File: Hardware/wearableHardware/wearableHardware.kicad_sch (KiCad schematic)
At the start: 0 parts

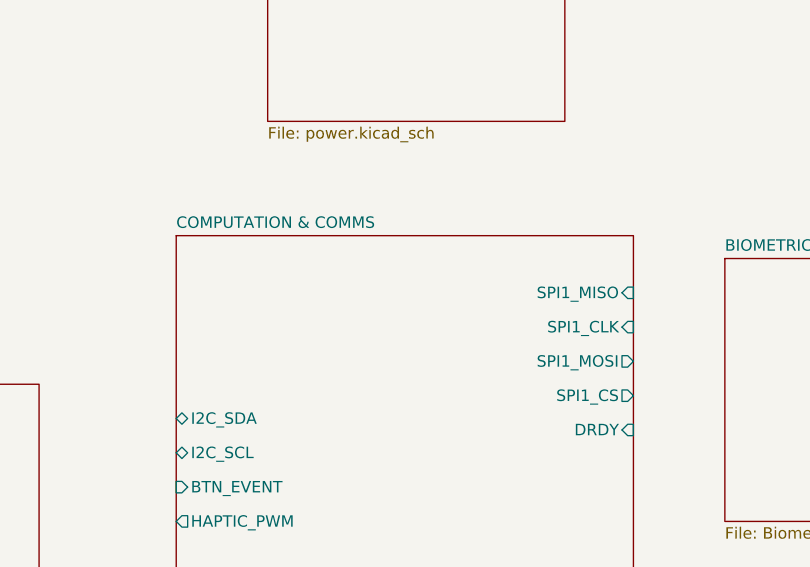
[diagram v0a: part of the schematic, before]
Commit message: feat: initialize KiCad hardware project with MCU schematic and pinmap configuration
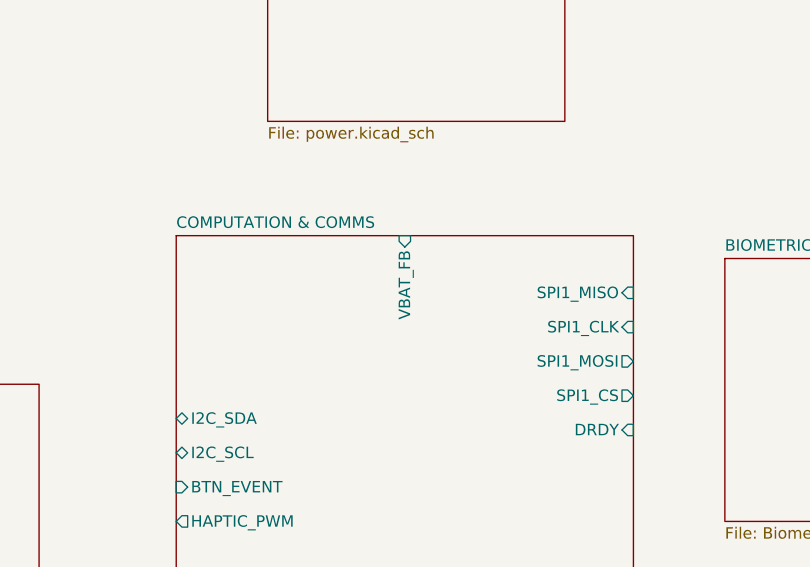
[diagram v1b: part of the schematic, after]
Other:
- sheet COMPUTATION & COMMS ports: added VBAT_FB; removed none
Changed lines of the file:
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@@
+			)
+		)
+		(pin "VBAT_FB" input
+			(at 128.27 58.42 90)
+			(effects
+				(font
+					(size 1.27 1.27)
+				)
+				(justify right)
 			)
 		)

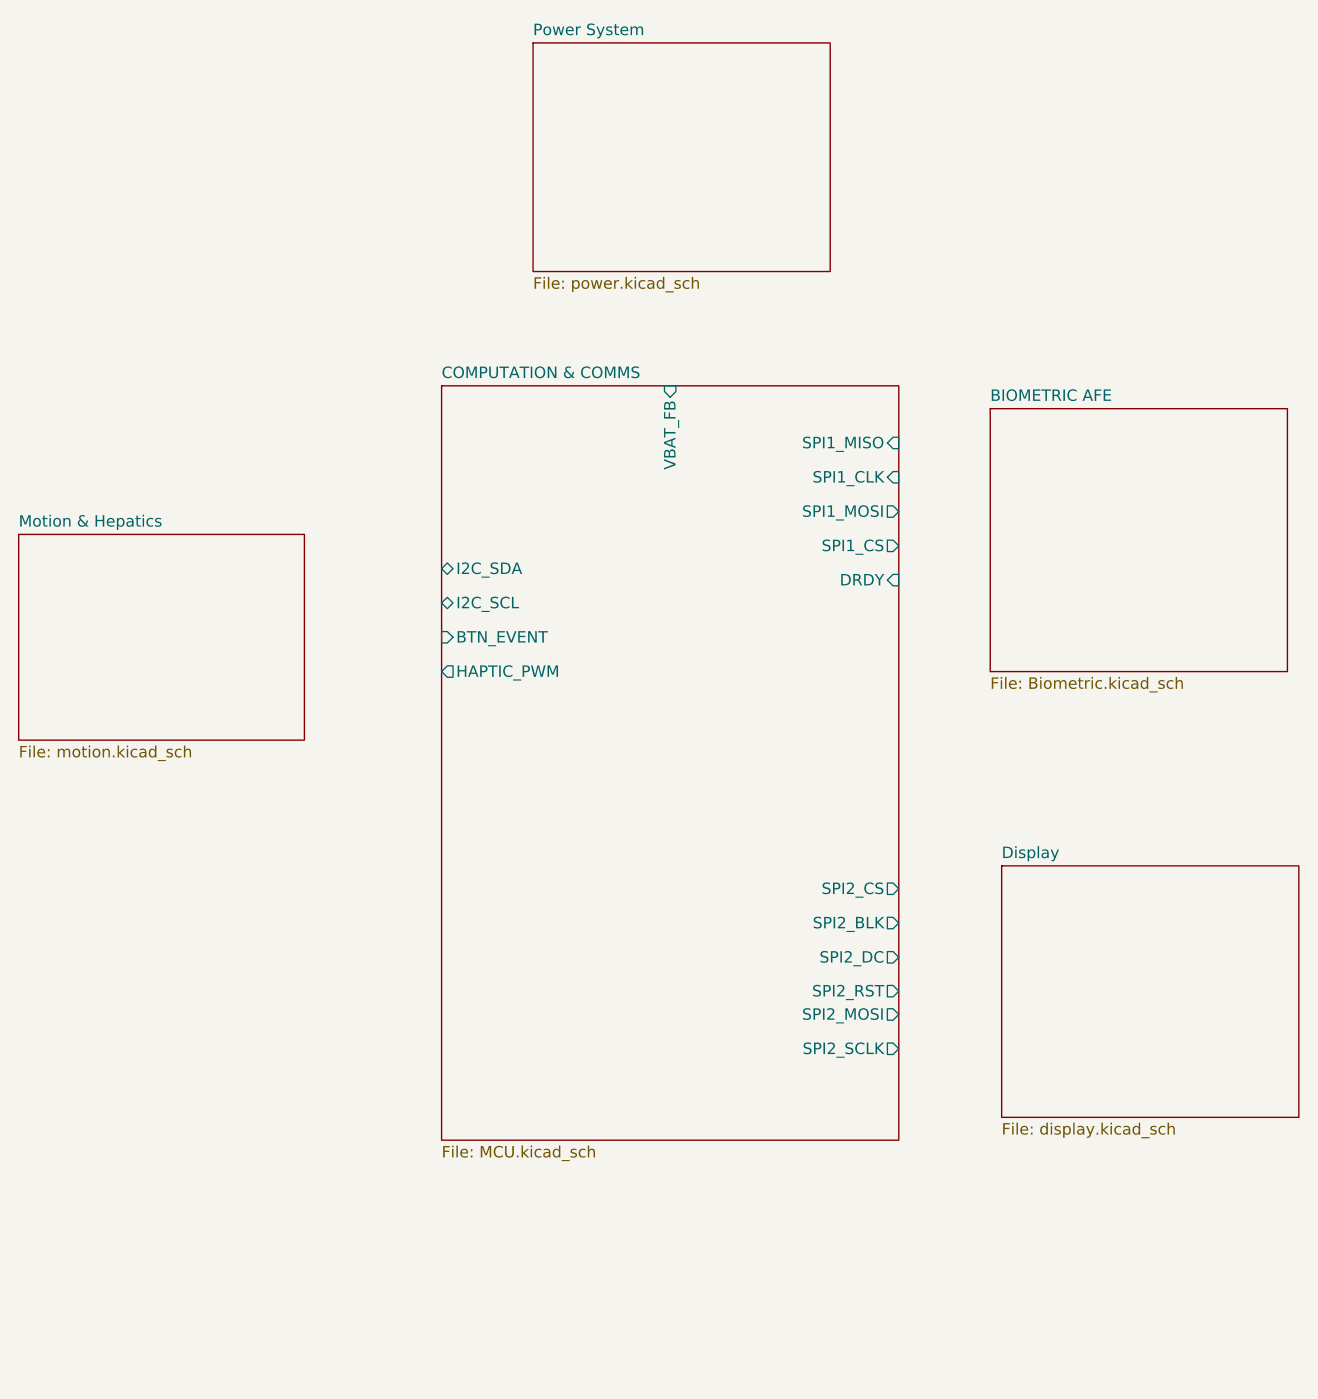
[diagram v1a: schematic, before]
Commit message: feat: add hardware schematics, documentation images, and external component libraries for wearable device development
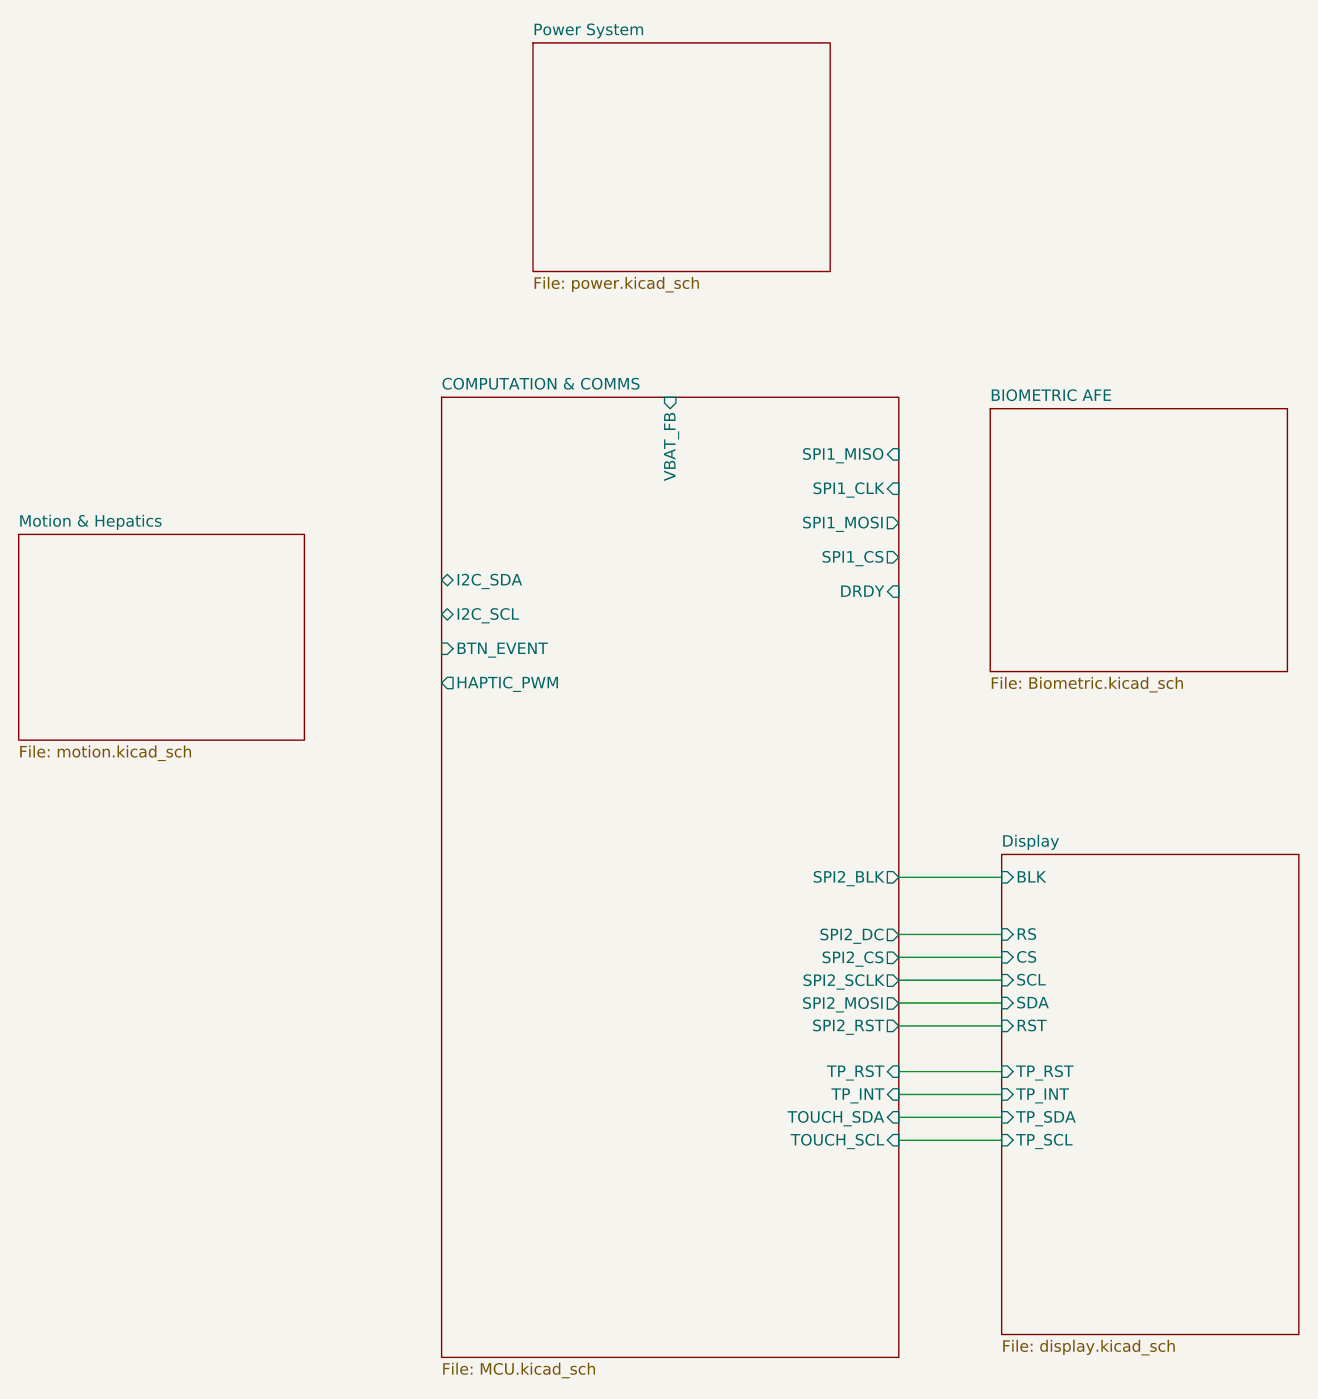
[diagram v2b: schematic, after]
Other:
- sheet COMPUTATION & COMMS ports: added TOUCH_SCL, TOUCH_SDA, TP_INT, TP_RST; removed none
- sheet Display ports: added BLK, CS, RS, RST, SCL, SDA, TP_INT, TP_RST, TP_SCL, TP_SDA; removed none
